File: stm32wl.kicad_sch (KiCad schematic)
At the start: 25 parts, among them U201 STM32WLE5CCUx

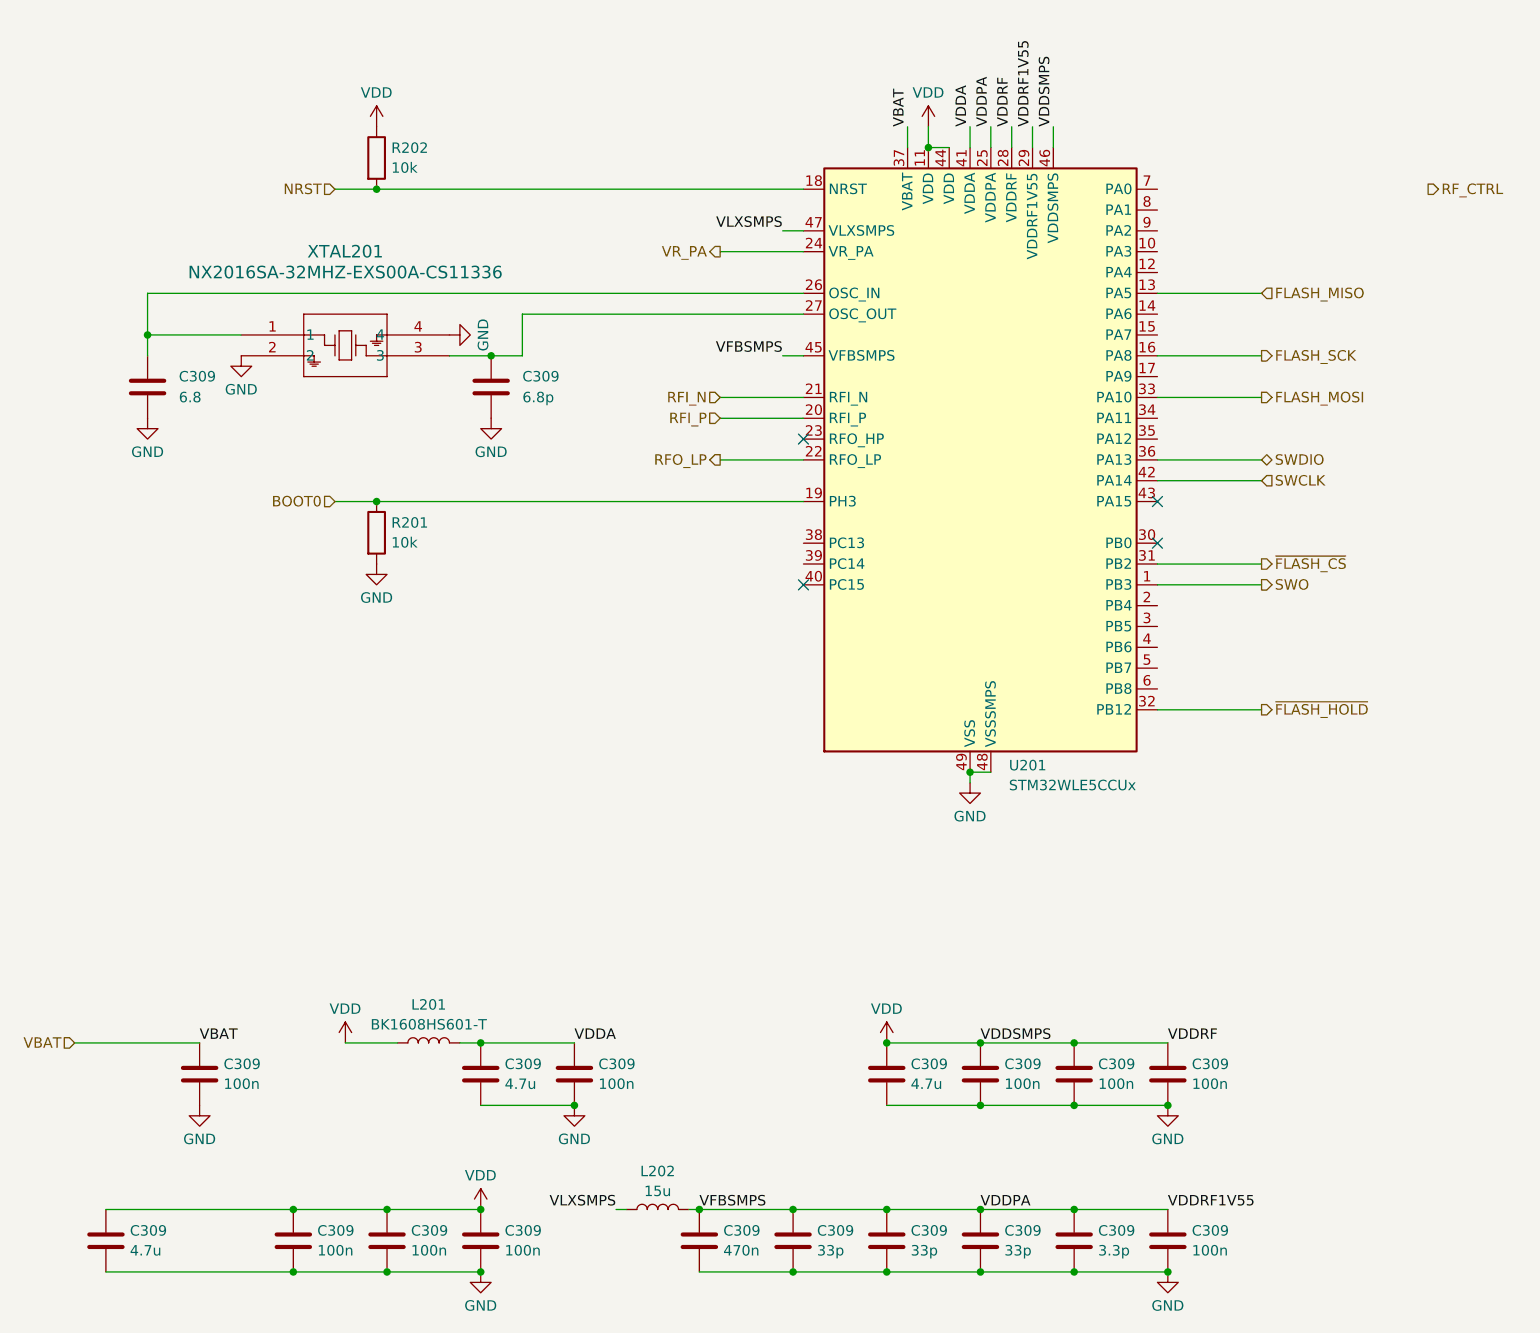
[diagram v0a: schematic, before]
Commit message: mostly finishing, all IOs connected, drc clean
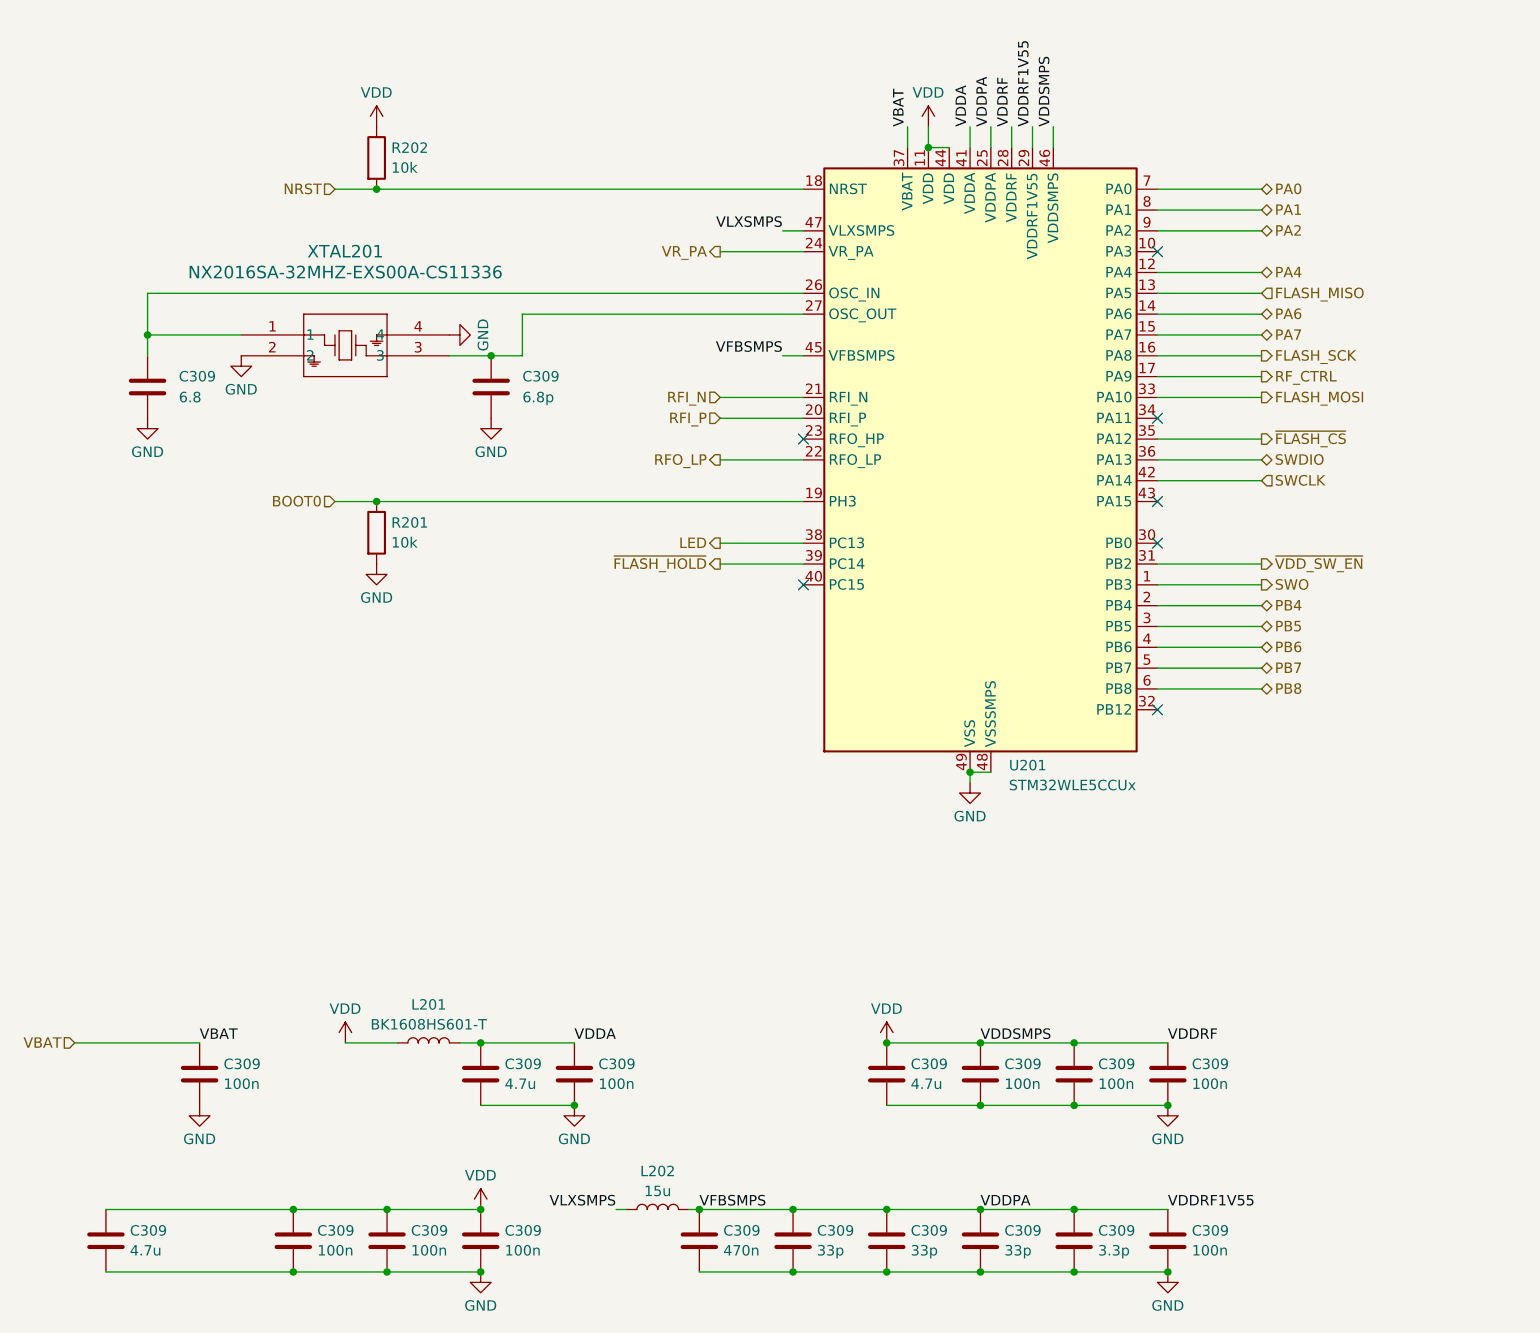
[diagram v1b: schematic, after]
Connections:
- net RF_CTRL: now also U201.17 (PA9)
- net ~{FLASH_CS}: now also U201.35 (PA12); no longer U201.31 (PB2)
- net ~{FLASH_HOLD}: now also U201.39 (PC14); no longer U201.32 (PB12)
- net PA4: now reaches U201.12 (PA4)
- net PA6: now reaches U201.14 (PA6)
- net PA7: now reaches U201.15 (PA7)
- net PB4: now reaches U201.2 (PB4)
- net PB5: now reaches U201.3 (PB5)
- net LED: now reaches U201.38 (PC13)
- net PB6: now reaches U201.4 (PB6)
- net PB7: now reaches U201.5 (PB7)
- net PB8: now reaches U201.6 (PB8)
- net PA0: now reaches U201.7 (PA0)
- net PA1: now reaches U201.8 (PA1)
- net PA2: now reaches U201.9 (PA2)
- new net ~{VDD_SW_EN}: U201.31 (PB2)
- no-connect marks 4 -> 7
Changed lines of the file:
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@@
   (junction (at 148.59 189.23) (diameter 0) (color 0 0 0 0)
   )
+  (no_connect (at 158.75 85.09))
   (no_connect (at 115.57 105.41))
+  (no_connect (at 158.75 64.77))
   (no_connect (at 115.57 87.63))
   (no_connect (at 158.75 95.25))
   (no_connect (at 158.75 100.33))
+  (no_connect (at 158.75 120.65))
+  (wire (pts (xy 105.41 102.87) (xy 115.57 102.87))
+    (stroke (width 0) (type default))
+  )
   (wire (pts (xy 35.56 74.93) (xy 35.56 69.85))
     (stroke (width 0) (type default))
@@
     (stroke (width 0) (type default))
   )
+  (wire (pts (xy 158.75 80.01) (xy 171.45 80.01))
+    (stroke (width 0) (type default))
+  )
+  (wire (pts (xy 158.75 110.49) (xy 171.45 110.49))
+    (stroke (width 0) (type default))
+  )
   (wire (pts (xy 146.05 49.53) (xy 146.05 52.07))
     (stroke (width 0) (type default))
@@
     (stroke (width 0) (type default))
   )
+  (wire (pts (xy 158.75 72.39) (xy 171.45 72.39))
+    (stroke (width 0) (type default))
+  )
   (wire (pts (xy 35.56 69.85) (xy 115.57 69.85))
     (stroke (width 0) (type default))
@@
     (stroke (width 0) (type default))
   )
+  (wire (pts (xy 158.75 113.03) (xy 171.45 113.03))
+    (stroke (width 0) (type default))
+  )
   (wire (pts (xy 105.41 85.09) (xy 115.57 85.09))
     (stroke (width 0) (type default))
   )
+  (wire (pts (xy 158.75 59.69) (xy 171.45 59.69))
+    (stroke (width 0) (type default))
+  )
   (wire (pts (xy 76.2 168.91) (xy 87.63 168.91))
     (stroke (width 0) (type default))
@@
     (stroke (width 0) (type default))
   )
+  (wire (pts (xy 158.75 107.95) (xy 171.45 107.95))
+    (stroke (width 0) (type default))
+  )
   (wire (pts (xy 26.67 161.29) (xy 41.91 161.29))
     (stroke (width 0) (type default))
@@
     (stroke (width 0) (type default))
   )
+  (wire (pts (xy 158.75 118.11) (xy 171.45 118.11))
+    (stroke (width 0) (type default))
+  )
   (wire (pts (xy 158.75 69.85) (xy 171.45 69.85))
     (stroke (width 0) (type default))
@@
     (stroke (width 0) (type default))
   )
+  (wire (pts (xy 158.75 67.31) (xy 171.45 67.31))
+    (stroke (width 0) (type default))
+  )
   (wire (pts (xy 160.02 161.29) (xy 148.59 161.29))
     (stroke (width 0) (type default))
   )
+  (wire (pts (xy 158.75 115.57) (xy 171.45 115.57))
+    (stroke (width 0) (type default))
+  )
   (wire (pts (xy 53.34 181.61) (xy 64.77 181.61))
     (stroke (width 0) (type default))
   )
+  (wire (pts (xy 105.41 100.33) (xy 115.57 100.33))
+    (stroke (width 0) (type default))
+  )
   (wire (pts (xy 30.48 189.23) (xy 53.34 189.23))
     (stroke (width 0) (type default))
@@
     (stroke (width 0) (type default))
   )
+  (wire (pts (xy 158.75 62.23) (xy 171.45 62.23))
+    (stroke (width 0) (type default))
+  )
+  (wire (pts (xy 158.75 57.15) (xy 171.45 57.15))
+    (stroke (width 0) (type default))
+  )
   (wire (pts (xy 35.56 77.47) (xy 35.56 74.93))
     (stroke (width 0) (type default))
@@
     (stroke (width 0) (type default))
   )
+  (wire (pts (xy 158.75 87.63) (xy 171.45 87.63))
+    (stroke (width 0) (type default))
+  )
   (wire (pts (xy 105.41 64.77) (xy 115.57 64.77))
     (stroke (width 0) (type default))
   )
+  (wire (pts (xy 158.75 74.93) (xy 171.45 74.93))
+    (stroke (width 0) (type default))
+  )
   (wire (pts (xy 113.03 77.47) (xy 115.57 77.47))
     (stroke (width 0) (type default))
   )
   (wire (pts (xy 158.75 92.71) (xy 171.45 92.71))
-    (stroke (width 0) (type default))
-  )
-  (wire (pts (xy 158.75 120.65) (xy 171.45 120.65))
     (stroke (width 0) (type default))
   )
@@
     (effects (font (size 1.27 1.27)) (justify left bottom))
   )
-  (hierarchical_label "~{FLASH_CS}" (shape output) (at 171.45 102.87 0) (fields_autoplaced)
+  (hierarchical_label "~{VDD_SW_EN}" (shape output) (at 171.45 102.87 0) (fields_autoplaced)
+    (effects (font (size 1.27 1.27)) (justify left))
+  )
+  (hierarchical_label "~{FLASH_CS}" (shape output) (at 171.45 87.63 0) (fields_autoplaced)
     (effects (font (size 1.27 1.27)) (justify left))
   )
@@
     (effects (font (size 1.27 1.27)) (justify right))
   )
+  (hierarchical_label "PA4" (shape bidirectional) (at 171.45 67.31 0) (fields_autoplaced)
+    (effects (font (size 1.27 1.27)) (justify left))
+  )
+  (hierarchical_label "PB6" (shape bidirectional) (at 171.45 113.03 0) (fields_autoplaced)
+    (effects (font (size 1.27 1.27)) (justify left))
+  )
   (hierarchical_label "SWCLK" (shape input) (at 171.45 92.71 0) (fields_autoplaced)
     (effects (font (size 1.27 1.27)) (justify left))
@@
     (effects (font (size 1.27 1.27)) (justify right))
   )
-  (hierarchical_label "RF_CTRL" (shape output) (at 191.77 57.15 0) (fields_autoplaced)
+  (hierarchical_label "PB8" (shape bidirectional) (at 171.45 118.11 0) (fields_autoplaced)
+    (effects (font (size 1.27 1.27)) (justify left))
+  )
+  (hierarchical_label "PA7" (shape bidirectional) (at 171.45 74.93 0) (fields_autoplaced)
+    (effects (font (size 1.27 1.27)) (justify left))
+  )
+  (hierarchical_label "RF_CTRL" (shape output) (at 171.45 80.01 0) (fields_autoplaced)
     (effects (font (size 1.27 1.27)) (justify left))
   )
@@
     (effects (font (size 1.27 1.27)) (justify left))
   )
-  (hierarchical_label "~{FLASH_HOLD}" (shape output) (at 171.45 120.65 0) (fields_autoplaced)
-    (effects (font (size 1.27 1.27)) (justify left))
+  (hierarchical_label "~{FLASH_HOLD}" (shape output) (at 105.41 102.87 180) (fields_autoplaced)
+    (effects (font (size 1.27 1.27)) (justify right))
   )
   (hierarchical_label "SWO" (shape output) (at 171.45 105.41 0) (fields_autoplaced)
     (effects (font (size 1.27 1.27)) (justify left))
   )
+  (hierarchical_label "LED" (shape output) (at 105.41 100.33 180) (fields_autoplaced)
+    (effects (font (size 1.27 1.27)) (justify right))
+  )
+  (hierarchical_label "PA6" (shape bidirectional) (at 171.45 72.39 0) (fields_autoplaced)
+    (effects (font (size 1.27 1.27)) (justify left))
+  )
   (hierarchical_label "NRST" (shape input) (at 58.42 57.15 180) (fields_autoplaced)
     (effects (font (size 1.27 1.27)) (justify right))
   )
+  (hierarchical_label "PB7" (shape bidirectional) (at 171.45 115.57 0) (fields_autoplaced)
+    (effects (font (size 1.27 1.27)) (justify left))
+  )
   (hierarchical_label "SWDIO" (shape bidirectional) (at 171.45 90.17 0) (fields_autoplaced)
     (effects (font (size 1.27 1.27)) (justify left))
@@
     (effects (font (size 1.27 1.27)) (justify right))
   )
+  (hierarchical_label "PA0" (shape bidirectional) (at 171.45 57.15 0) (fields_autoplaced)
+    (effects (font (size 1.27 1.27)) (justify left))
+  )
   (hierarchical_label "VR_PA" (shape output) (at 105.41 64.77 180) (fields_autoplaced)
     (effects (font (size 1.27 1.27)) (justify right))
   )
+  (hierarchical_label "PB4" (shape bidirectional) (at 171.45 107.95 0) (fields_autoplaced)
+    (effects (font (size 1.27 1.27)) (justify left))
+  )
+  (hierarchical_label "PA2" (shape bidirectional) (at 171.45 62.23 0) (fields_autoplaced)
+    (effects (font (size 1.27 1.27)) (justify left))
+  )
+  (hierarchical_label "PA1" (shape bidirectional) (at 171.45 59.69 0) (fields_autoplaced)
+    (effects (font (size 1.27 1.27)) (justify left))
+  )
+  (hierarchical_label "PB5" (shape bidirectional) (at 171.45 110.49 0) (fields_autoplaced)
+    (effects (font (size 1.27 1.27)) (justify left))
+  )
   (hierarchical_label "FLASH_SCK" (shape output) (at 171.45 77.47 0) (fields_autoplaced)

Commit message: groundplane settings tweak
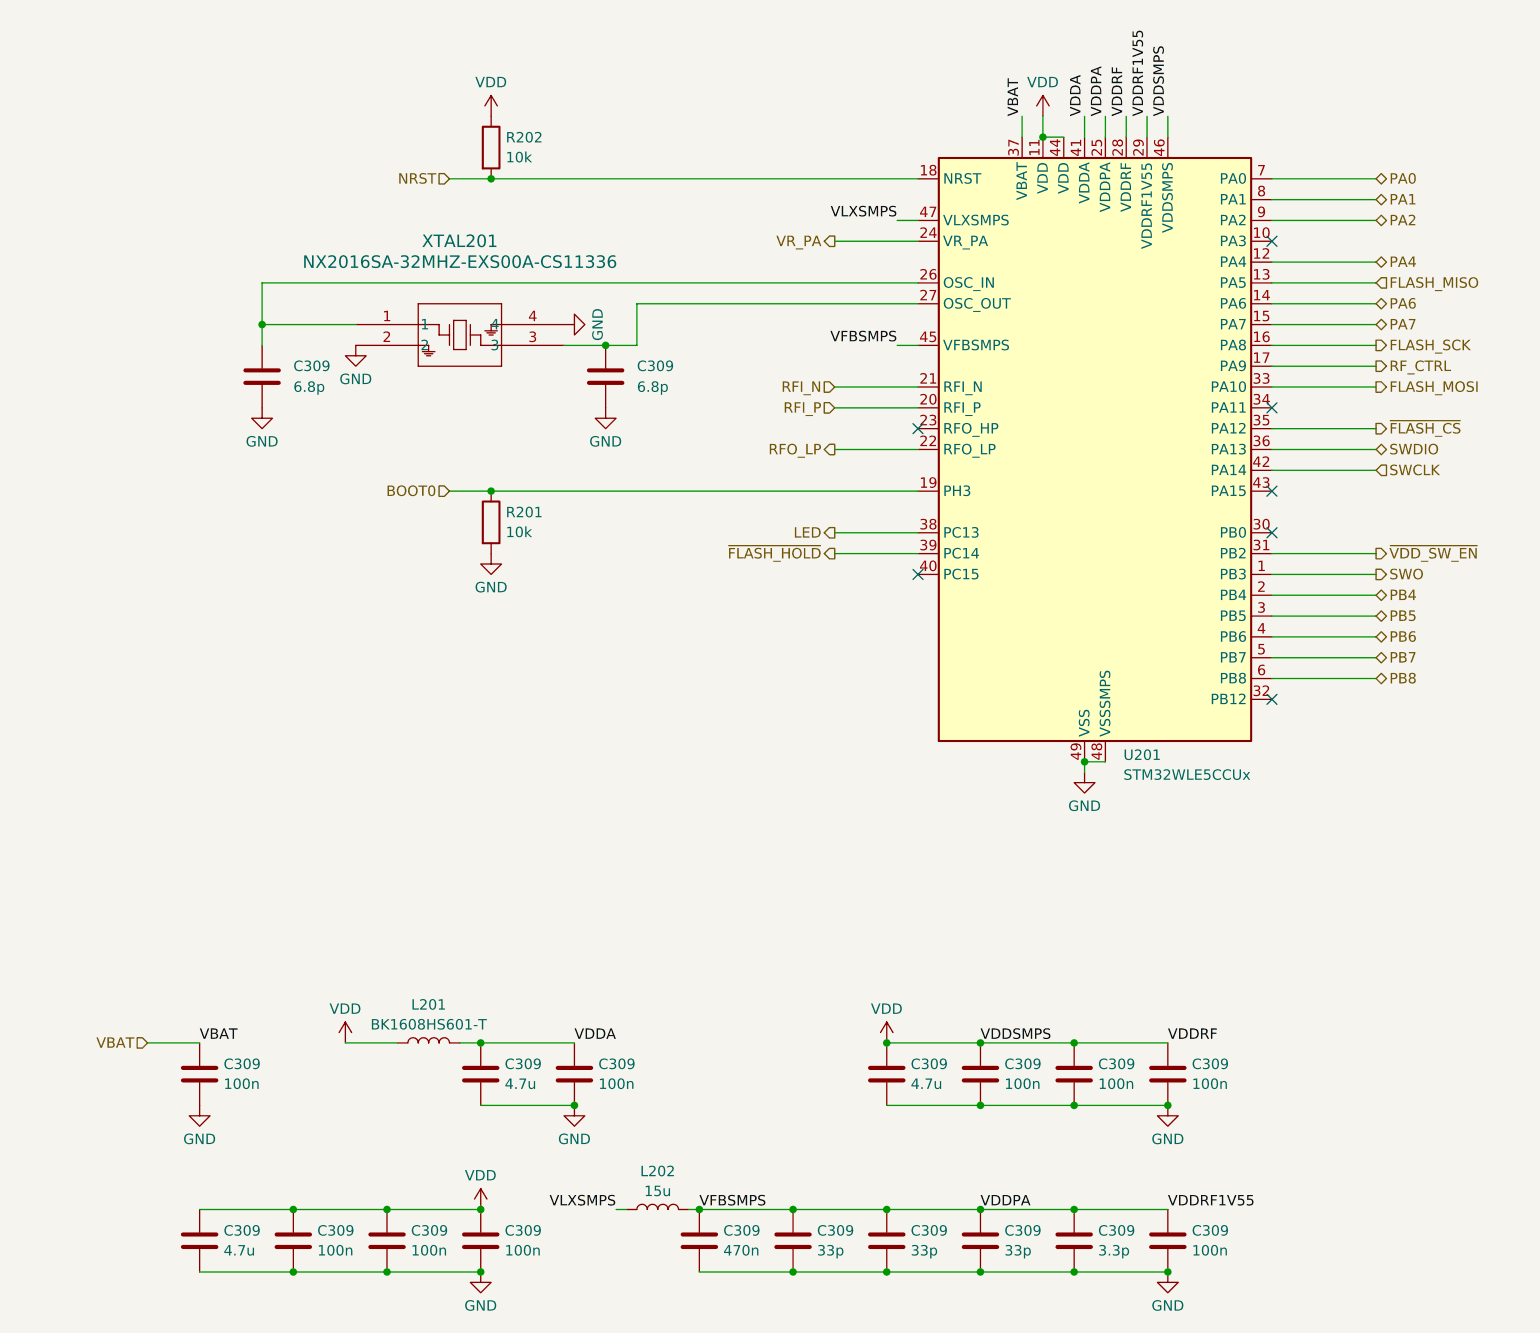
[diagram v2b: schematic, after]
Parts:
- C309: value 6.8 -> 6.8p
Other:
- moved on the sheet: C309, R201, R202, U201, XTAL201
